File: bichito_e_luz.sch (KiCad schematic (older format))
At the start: 3 parts, among them J1 USB_OTG

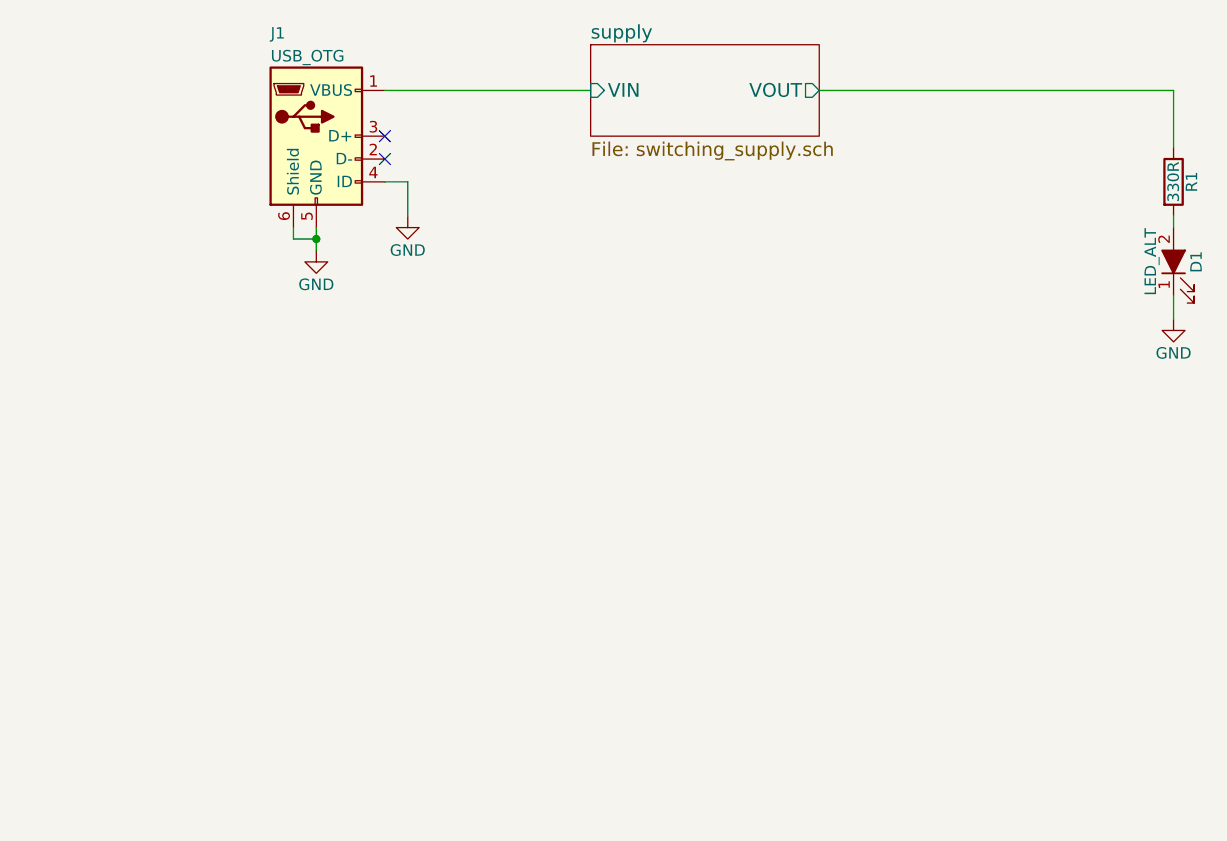
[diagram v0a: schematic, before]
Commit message: Esquematico completo. Footprintss asignados
Signed-off-by: Marcos Chaparro <mchaparro@paltatech.com>
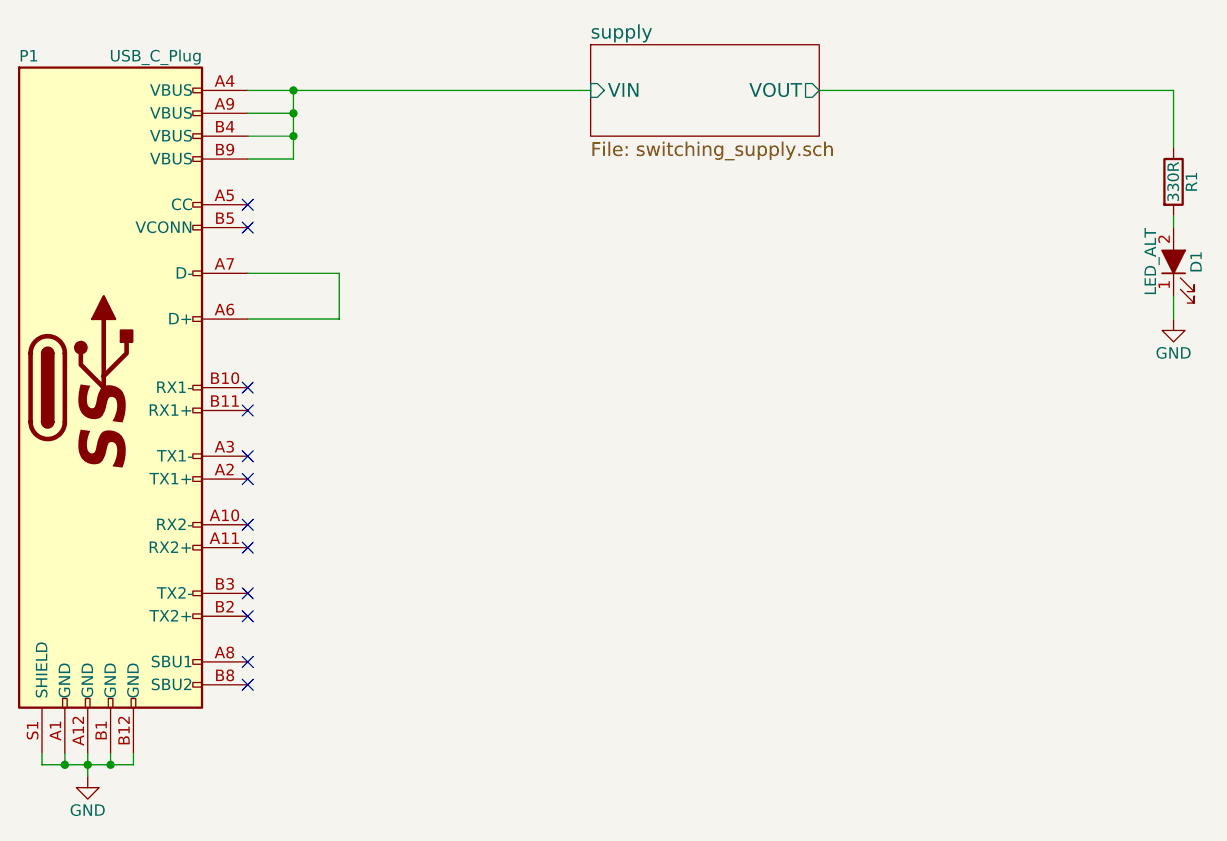
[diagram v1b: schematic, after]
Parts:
- removed J1: USB_OTG, symbol USB_OTG
- added P1: USB_C_Plug, Connectors_USB:USB_C_Plug_Molex_105444, symbol USB_C_Plug
- D1: footprint (none) -> LEDs:LED_Cree-XB; MPN (none) -> XBDAWT-00-0000-000000CE5
- R1: footprint (none) -> Resistors_SMD:R_1210
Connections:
- net GND: now also P1.A1 (GND), P1.A12 (GND), P1.B1 (GND), P1.B12 (GND), P1.S1 (SHIELD)
- net supply/VIN: now also P1.A4 (VBUS), P1.A9 (VBUS), P1.B4 (VBUS), P1.B9 (VBUS)
- new net: P1.A6 (D+), P1.A7 (D-)
- no-connect marks 2 -> 12
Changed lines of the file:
@@
 LIBS:contrib
 LIBS:valves
+LIBS:curso
+LIBS:bichito_e_luz-cache
 EELAYER 25 0
 EELAYER END
@@
 F 0 "D1" H 7050 3400 50  0000 C CNN
 F 1 "LED_ALT" H 7050 3600 50  0000 C CNN
-F 2 "" H 7050 3500 50  0001 C CNN
+F 2 "LEDs:LED_Cree-XB" H 7050 3500 50  0001 C CNN
 F 3 "" H 7050 3500 50  0001 C CNN
+F 4 "XBDAWT-00-0000-000000CE5" H 7050 3500 60  0001 C CNN "MPN"
 	1    7050 3500
 	0    -1   -1   0
@@
 	1    0    0    -1
 $EndComp
-$Comp
-L USB_OTG J1
-U 1 1 59AF06F8
-P 3300 2950
-F 0 "J1" H 3100 3400 50  0000 L CNN
-F 1 "USB_OTG" H 3100 3300 50  0000 L CNN
-F 2 "" H 3450 2900 50  0001 C CNN
-F 3 "" H 3450 2900 50  0001 C CNN
-	1    3300 2950
-	1    0    0    -1
-$EndComp
-$Comp
-L GND #PWR02
-U 1 1 59AF0777
-P 3300 3450
-F 0 "#PWR02" H 3300 3200 50  0001 C CNN
-F 1 "GND" H 3300 3300 50  0000 C CNN
-F 2 "" H 3300 3450 50  0001 C CNN
-F 3 "" H 3300 3450 50  0001 C CNN
-	1    3300 3450
-	1    0    0    -1
-$EndComp
 Wire Wire Line
 	7050 3650 7050 3750
-Wire Wire Line
-	3200 3350 3200 3400
-Wire Wire Line
-	3200 3400 3300 3400
-Wire Wire Line
-	3300 3350 3300 3450
-Connection ~ 3300 3400
 $Comp
 L R R1
@@
 F 0 "R1" V 7130 3150 50  0000 C CNN
 F 1 "330R" V 7050 3150 50  0000 C CNN
-F 2 "" V 6980 3150 50  0001 C CNN
+F 2 "Resistors_SMD:R_1210" V 6980 3150 50  0001 C CNN
 F 3 "" H 7050 3150 50  0001 C CNN
 F 4 "completar" V 7050 3150 60  0001 C CNN "MPN"
@@
 Wire Wire Line
 	7050 3000 7050 2750
-Wire Wire Line
-	3600 3150 3700 3150
-Wire Wire Line
-	3700 3150 3700 3300
-$Comp
-L GND #PWR03
-U 1 1 59AF0B16
-P 3700 3300
-F 0 "#PWR03" H 3700 3050 50  0001 C CNN
-F 1 "GND" H 3700 3150 50  0000 C CNN
-F 2 "" H 3700 3300 50  0001 C CNN
-F 3 "" H 3700 3300 50  0001 C CNN
-	1    3700 3300
-	1    0    0    -1
-$EndComp
-NoConn ~ 3600 2950
-NoConn ~ 3600 3050
 $Sheet
 S 4500 2550 1000 400
@@
 $EndSheet
 Wire Wire Line
-	3600 2750 4500 2750
+	3000 2750 4500 2750
 Wire Wire Line
 	7050 2750 5500 2750
+$Comp
+L USB_C_Plug P1
+U 1 1 59B19F80
+P 2400 4050
+F 0 "P1" H 2000 5500 50  0000 L CNN
+F 1 "USB_C_Plug" H 2800 5500 50  0000 R CNN
+F 2 "Connectors_USB:USB_C_Plug_Molex_105444" H 2550 4050 50  0001 C CNN
+F 3 "" H 2550 4050 50  0001 C CNN
+	1    2400 4050
+	1    0    0    -1
+$EndComp
+Wire Wire Line
+	3000 2850 3200 2850
+Wire Wire Line
+	3200 2750 3200 3050
+Connection ~ 3200 2750
+Wire Wire Line
+	3200 2950 3000 2950
+Connection ~ 3200 2850
+Wire Wire Line
+	3200 3050 3000 3050
+Connection ~ 3200 2950
+$Comp
+L GND #PWR02
+U 1 1 59B1A165
+P 2300 5750
+F 0 "#PWR02" H 2300 5500 50  0001 C CNN
+F 1 "GND" H 2300 5600 50  0000 C CNN
+F 2 "" H 2300 5750 50  0001 C CNN
+F 3 "" H 2300 5750 50  0001 C CNN
+	1    2300 5750
+	1    0    0    -1
+$EndComp
+Wire Wire Line
+	2300 5750 2300 5650
+Wire Wire Line
+	2200 5650 2200 5700
+Wire Wire Line
+	2100 5700 2500 5700
+Connection ~ 2300 5700
+Wire Wire Line
+	2400 5700 2400 5650
+Wire Wire Line
+	2500 5700 2500 5650
+Connection ~ 2400 5700
+Wire Wire Line
+	3000 3750 3400 3750
+Wire Wire Line
+	3400 3750 3400 3550
+Wire Wire Line
+	3400 3550 3000 3550
+Wire Wire Line
+	2100 5650 2100 5700
+Connection ~ 2200 5700
+NoConn ~ 3000 3250
+NoConn ~ 3000 3350
+NoConn ~ 3000 4050
+NoConn ~ 3000 4150
+NoConn ~ 3000 4350
+NoConn ~ 3000 4450
+NoConn ~ 3000 4650
+NoConn ~ 3000 4750
+NoConn ~ 3000 4950
+NoConn ~ 3000 5050
+NoConn ~ 3000 5250
+NoConn ~ 3000 5350
 $EndSCHEMATC

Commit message: Termino layout. Despues de la clase agregue silkscreens y un fusible
Signed-off-by: Marcos Chaparro <mchaparro@paltatech.com>
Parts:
- P1: MPN (none) -> 105444-0001
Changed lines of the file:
@@
 	1    0    0    -1
 $EndComp
-Wire Wire Line
-	7050 3650 7050 3750
 $Comp
 L R R1
@@
 	1    0    0    -1
 $EndComp
-Wire Wire Line
-	7050 3300 7050 3350
-Wire Wire Line
-	7050 3000 7050 2750
 $Sheet
 S 4500 2550 1000 400
@@
 F3 "VOUT" O R 5500 2750 60
 $EndSheet
-Wire Wire Line
-	3000 2750 4500 2750
-Wire Wire Line
-	7050 2750 5500 2750
 $Comp
 L USB_C_Plug P1
@@
 F 2 "Connectors_USB:USB_C_Plug_Molex_105444" H 2550 4050 50  0001 C CNN
 F 3 "" H 2550 4050 50  0001 C CNN
+F 4 "105444-0001" H 2400 4050 60  0001 C CNN "MPN"
 	1    2400 4050
 	1    0    0    -1
 $EndComp
+$Comp
+L GND #PWR02
+U 1 1 59B1A165
+P 2300 5750
+F 0 "#PWR02" H 2300 5500 50  0001 C CNN
+F 1 "GND" H 2300 5600 50  0000 C CNN
+F 2 "" H 2300 5750 50  0001 C CNN
+F 3 "" H 2300 5750 50  0001 C CNN
+	1    2300 5750
+	1    0    0    -1
+$EndComp
+NoConn ~ 3000 3250
+NoConn ~ 3000 3350
+NoConn ~ 3000 4050
+NoConn ~ 3000 4150
+NoConn ~ 3000 4350
+NoConn ~ 3000 4450
+NoConn ~ 3000 4650
+NoConn ~ 3000 4750
+NoConn ~ 3000 4950
+NoConn ~ 3000 5050
+NoConn ~ 3000 5250
+NoConn ~ 3000 5350
+Wire Wire Line
+	7050 3650 7050 3750
+Wire Wire Line
+	7050 3300 7050 3350
+Wire Wire Line
+	7050 3000 7050 2750
+Wire Wire Line
+	3000 2750 4500 2750
+Wire Wire Line
+	7050 2750 5500 2750
 Wire Wire Line
 	3000 2850 3200 2850
@@
 	3200 3050 3000 3050
 Connection ~ 3200 2950
-$Comp
-L GND #PWR02
-U 1 1 59B1A165
-P 2300 5750
-F 0 "#PWR02" H 2300 5500 50  0001 C CNN
-F 1 "GND" H 2300 5600 50  0000 C CNN
-F 2 "" H 2300 5750 50  0001 C CNN
-F 3 "" H 2300 5750 50  0001 C CNN
-	1    2300 5750
-	1    0    0    -1
-$EndComp
 Wire Wire Line
-	2300 5750 2300 5650
+	2300 5650 2300 5750
 Wire Wire Line
 	2200 5650 2200 5700
@@
 	2100 5650 2100 5700
 Connection ~ 2200 5700
-NoConn ~ 3000 3250
-NoConn ~ 3000 3350
-NoConn ~ 3000 4050
-NoConn ~ 3000 4150
-NoConn ~ 3000 4350
-NoConn ~ 3000 4450
-NoConn ~ 3000 4650
-NoConn ~ 3000 4750
-NoConn ~ 3000 4950
-NoConn ~ 3000 5050
-NoConn ~ 3000 5250
-NoConn ~ 3000 5350
 $EndSCHEMATC

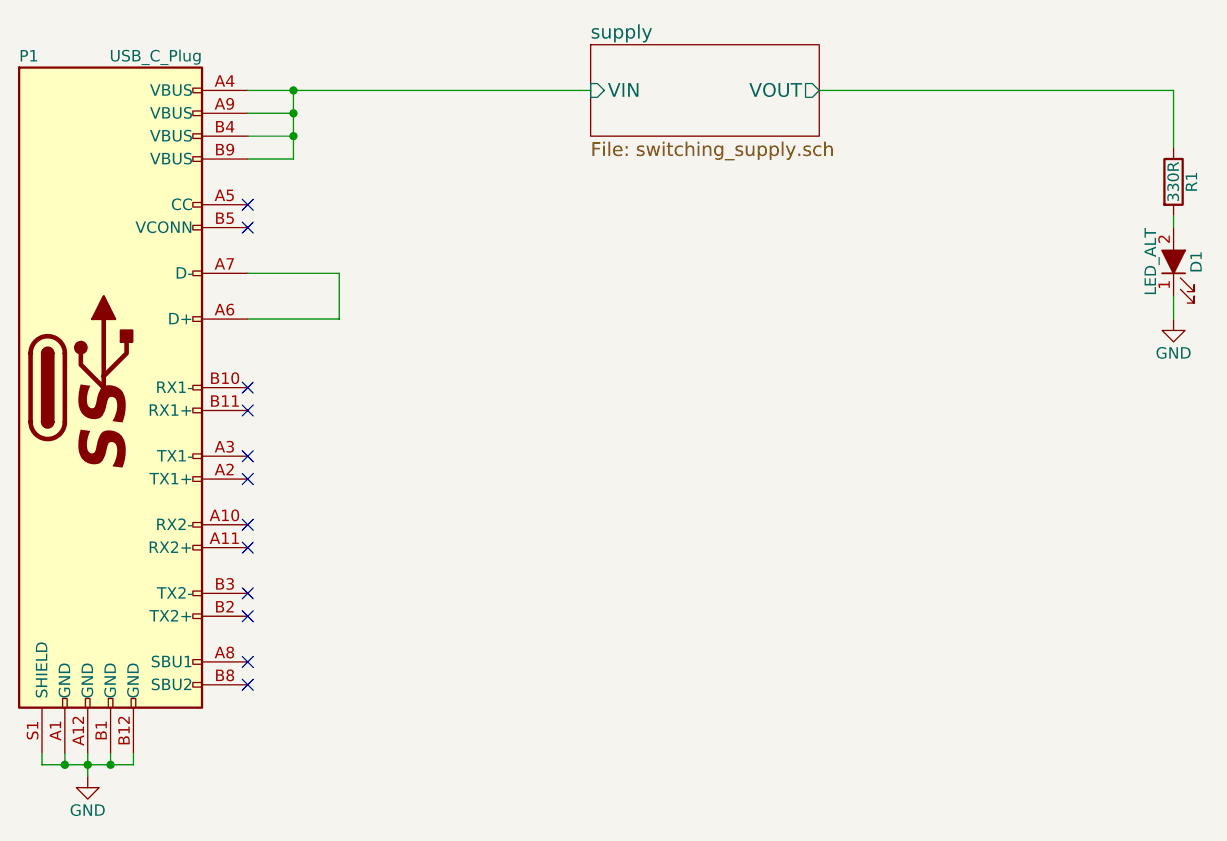
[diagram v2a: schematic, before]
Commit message: Add pulldowns updated values and assembly layer
Signed-off-by: Marcos Chaparro <mchaparro@paltatech.com>
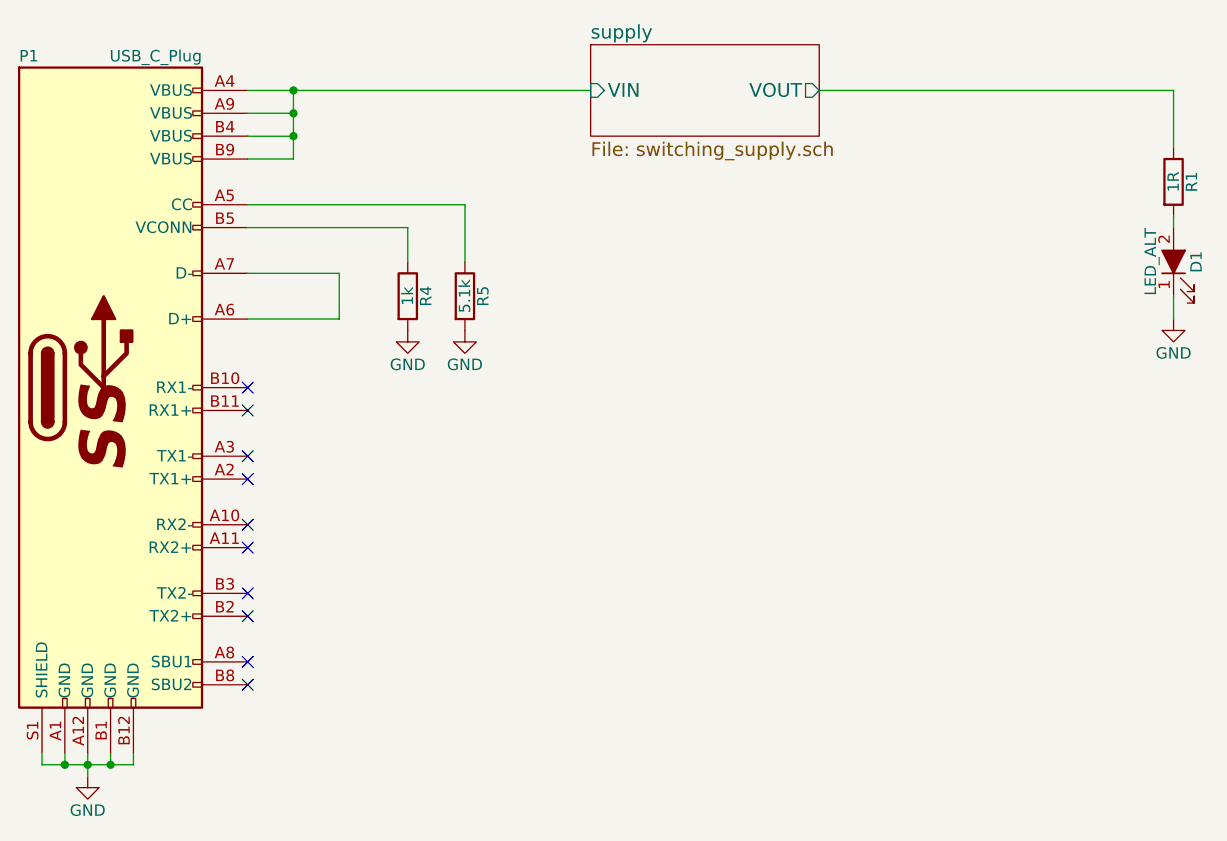
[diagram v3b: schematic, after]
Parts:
- added R4: 1k, Resistors_SMD:R_0603, symbol R
- added R5: 5.1k, Resistors_SMD:R_0603, symbol R
- R1: value 330R -> 1R; MPN completar -> RL1210FR-070R033L
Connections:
- net GND: now also R4.2, R5.2
- net at P1.A5 (CC): now also R5.1
- net at P1.B5 (VCONN): now also R4.1
- no-connect marks 12 -> 10
